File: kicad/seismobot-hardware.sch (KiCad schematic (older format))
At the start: 1 part

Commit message: raspberry pi header and mcu on schematic
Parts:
- added J?: Raspberry_Pi_2_3, symbol Connector:Raspberry_Pi_2_3
- added U?: STM32F051T8Yx, Package_CSP:ST_WLCSP-36_Die440, symbol MCU_ST_STM32F0:STM32F051T8Yx
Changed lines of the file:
@@
+	1    0    0    -1
+$EndComp
+$Comp
+L Connector:Raspberry_Pi_2_3 J?
+U 1 1 6092C0A8
+P 6300 3700
+F 0 "J?" H 6300 5181 50  0000 C CNN
+F 1 "Raspberry_Pi_2_3" H 6300 5090 50  0000 C CNN
+F 2 "" H 6300 3700 50  0001 C CNN
+F 3 "https://www.raspberrypi.org/documentation/hardware/raspberrypi/schematics/rpi_SCH_3bplus_1p0_reduced.pdf" H 6300 3700 50  0001 C CNN
+	1    6300 3700
+	1    0    0    -1
+$EndComp
+$Comp
+L MCU_ST_STM32F0:STM32F051T8Yx U?
+U 1 1 609309D2
+P 2250 2100
+F 0 "U?" H 2200 911 50  0000 C CNN
+F 1 "STM32F051T8Yx" H 2200 820 50  0000 C CNN
+F 2 "Package_CSP:ST_WLCSP-36_Die440" H 1750 1100 50  0001 R CNN
+F 3 "http://www.st.com/st-web-ui/static/active/en/resource/technical/document/datasheet/DM00039193.pdf" H 2250 2100 50  0001 C CNN
+	1    2250 2100
 	1    0    0    -1
 $EndComp

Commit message: add MCU (ATSAMD09) and supporting circuitry
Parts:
- removed U?: STM32F051T8Yx, Package_CSP:ST_WLCSP-36_Die440, symbol MCU_ST_STM32F0:STM32F051T8Yx
- added C?: 4.7 uF, symbol Device:C
- added C?: 0.1 uF, symbol Device:C
- added D?: LED, symbol Device:LED
- added R?: 1k, symbol Device:R
- added R?: 100, symbol Device:R
- added U?: ATSAMD09C13A-SS, Package_SO:SOIC-14_3.9x8.7mm_P1.27mm, symbol MCU_Microchip_SAMD:ATSAMD09C13A-SS
- added Y?: 32768 Hz, symbol Device:Crystal
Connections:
- net labels added: +3V3, CS, GND, MISO, MOSI, RX, RxD, SCK, SWCLK, SWDIO, TX, TxD, ~RST
- wire segments 0 -> 52
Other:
- moved on the sheet: J?, U?

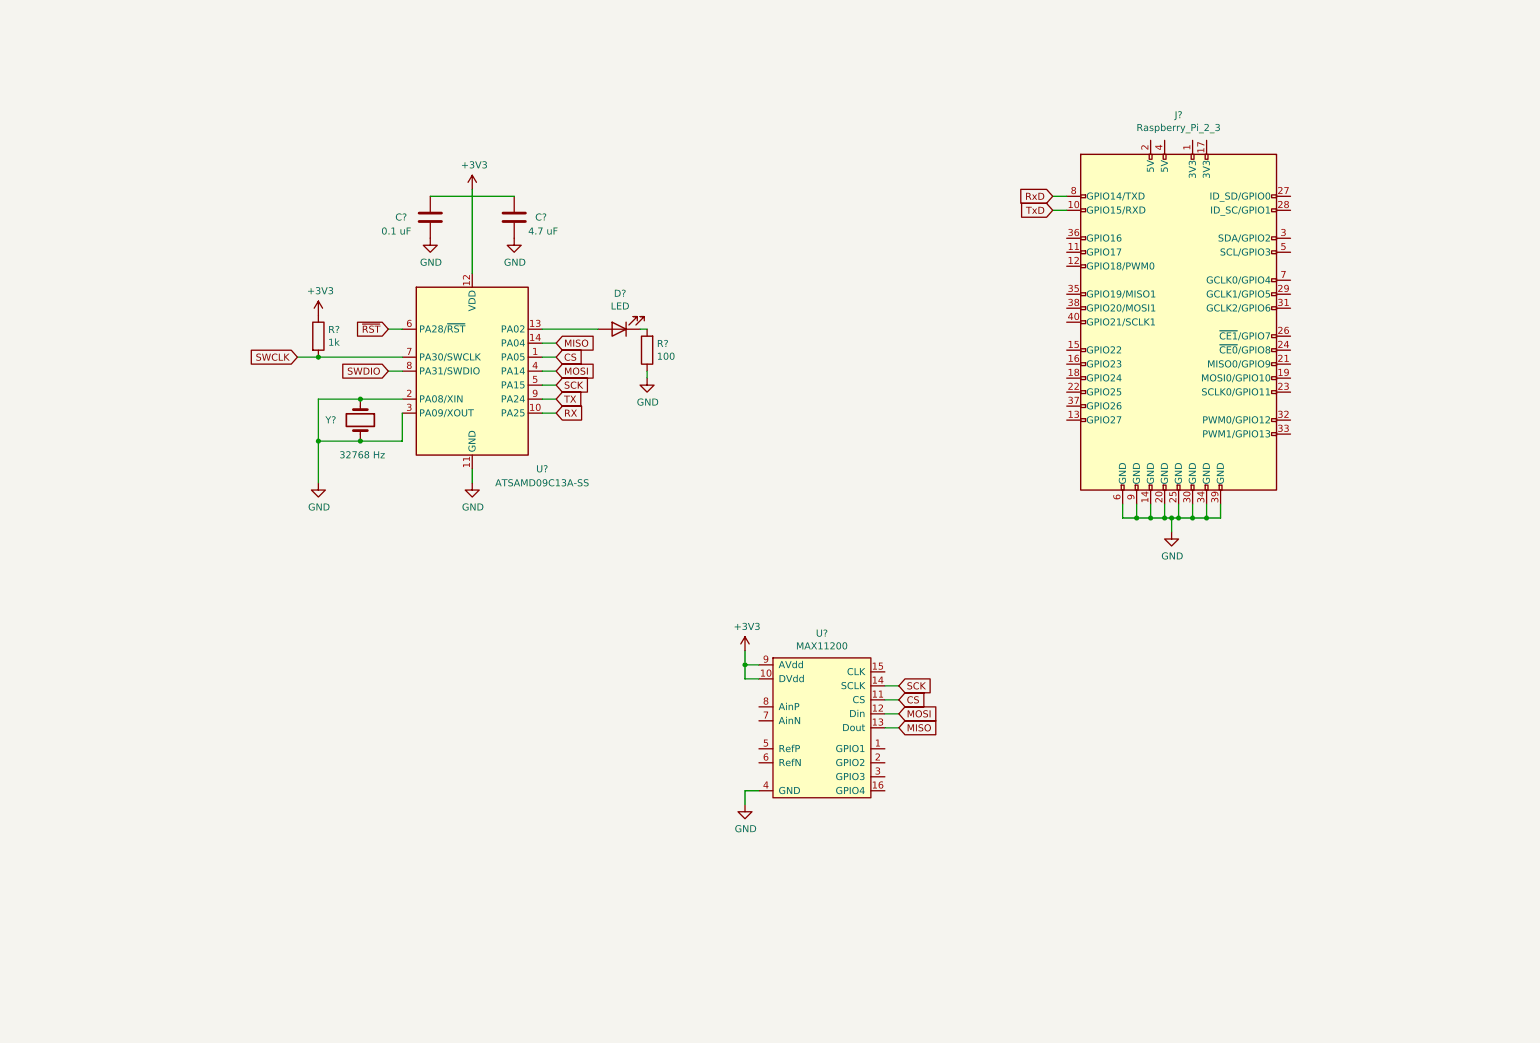
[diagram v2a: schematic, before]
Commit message: Added passives and clock to ADC
Based off of dev board
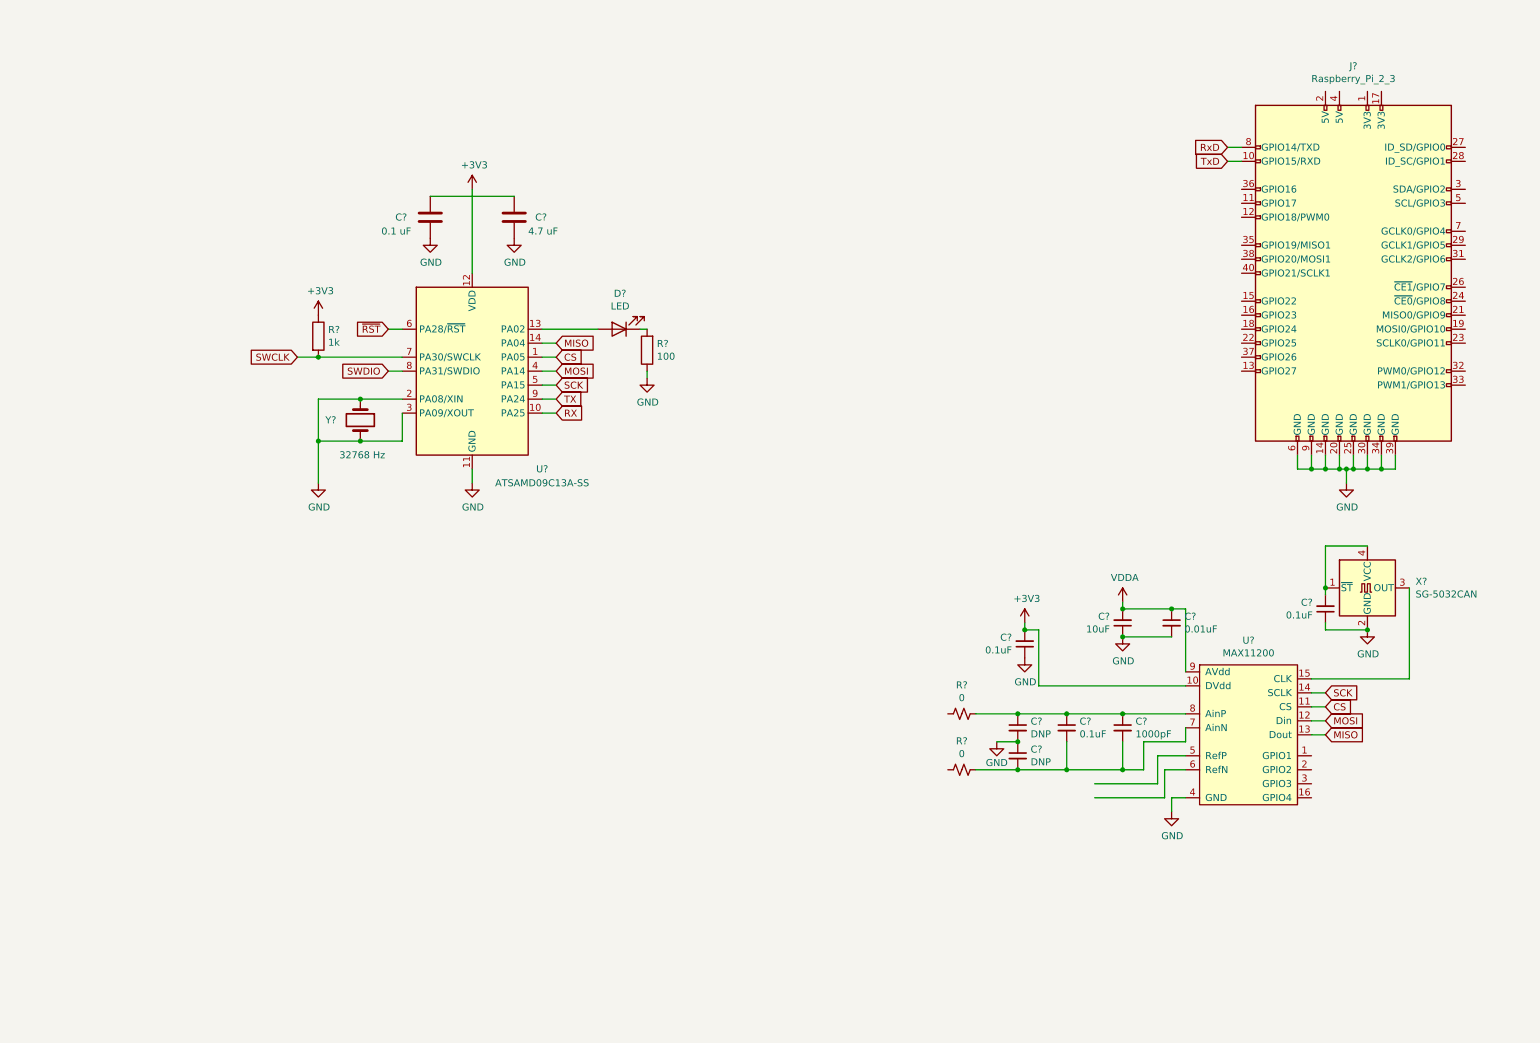
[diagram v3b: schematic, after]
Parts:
- added C?: 1000pF, symbol Device:C_Small
- added C? (x3): 0.1uF, symbol Device:C_Small
- added C?: 10uF, symbol Device:C_Small
- added C?: 0.01uF, symbol Device:C_Small
- added C? (x2): DNP, symbol Device:C_Small
- added R? (x2): 0, symbol Device:R_Small_US
- added X?: SG-5032CAN, Oscillator:Oscillator_SMD_SeikoEpson_SG8002LB-4Pin_5.0x3.2mm, symbol Oscillator:SG-5032CAN
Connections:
- net +3V3: now also C?.2; no longer U?.9 (AVdd)
- net GND: now also C?.1, C?.1, C?.1, C?.1, C?.2, C?.2, X?.2 (GND)
- net at U?.15 (CLK): now also X?.3 (OUT)
- net at U?.7 (AinN): now also C?.2, C?.2, C?.2, R?.1
- net at U?.8 (AinP): now also C?.1, C?.1, C?.1, R?.1
- new net: C?.2, X?.1 (~ST), X?.4 (VCC)
- new net VDDA: C?.1, C?.2, U?.9 (AVdd)
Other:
- moved on the sheet: J?, U?

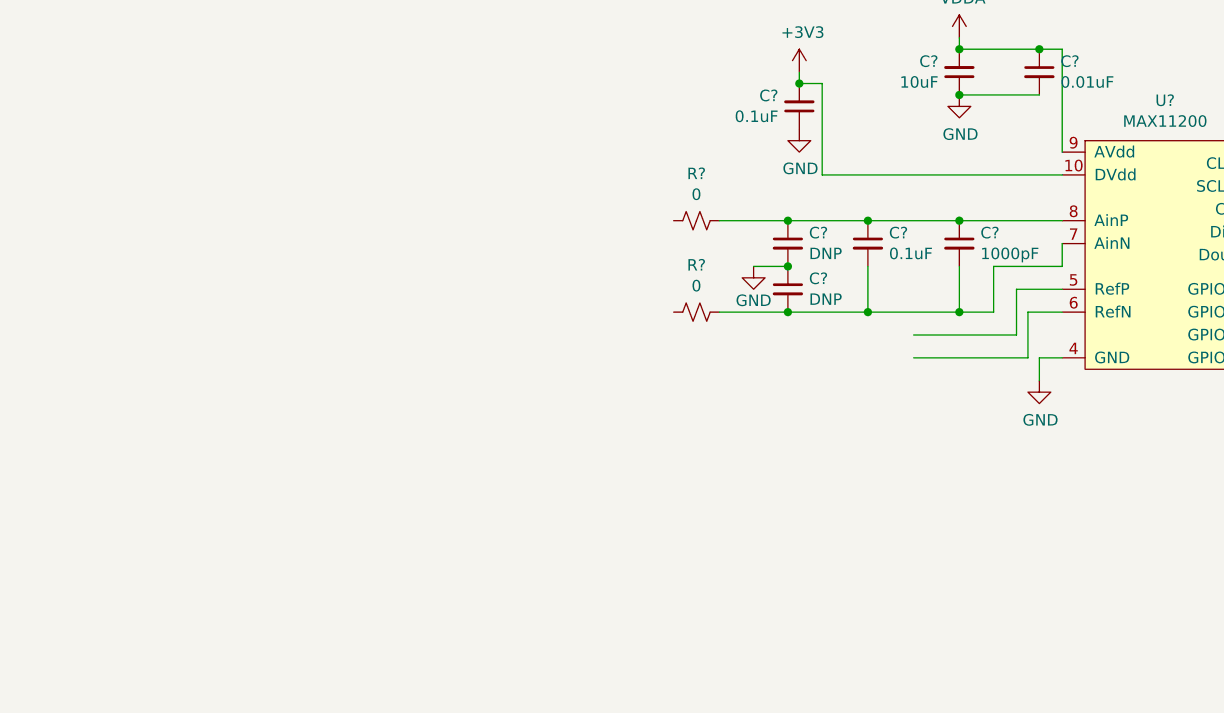
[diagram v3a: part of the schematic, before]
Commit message: added voltage references to schematic
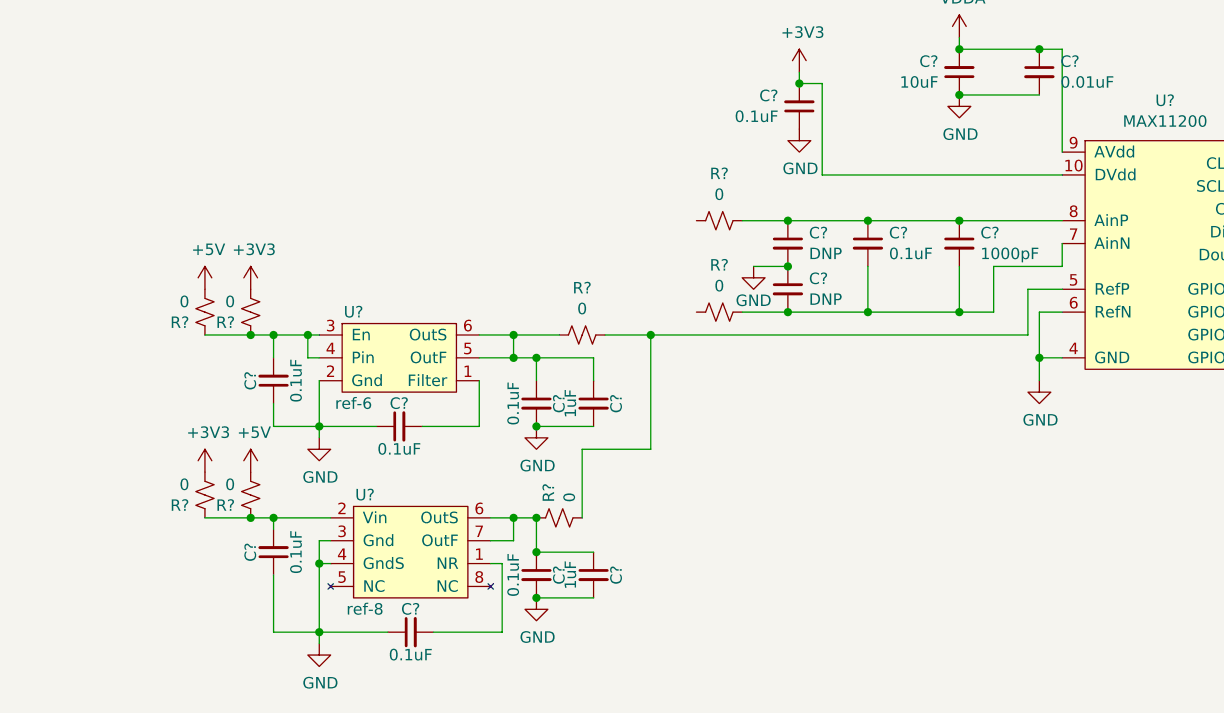
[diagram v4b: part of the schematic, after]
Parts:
- added C? (x6): 0.1uF, symbol Device:C_Small
- added C? (x2): 1uF, symbol Device:C_Small
- added R? (x6): 0, symbol Device:R_Small_US
- added U?: ref-6, symbol seismobot-hardware:ref-6
- added U?: ref-8, symbol seismobot-hardware:ref-8
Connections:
- net +3V3: now also R?.1, R?.1
- net GND: now also U?.6 (RefN), C?.1, C?.1, C?.1, C?.1, C?.2, C?.2, C?.2, C?.2, U?.2 (Gnd), U?.3 (Gnd), U?.4 (GndS)
- net at U?.5 (RefP): now also R?.1, R?.1
- new net: C?.2, U?.1 (Filter)
- new net: C?.2, R?.2, R?.2, U?.3 (En), U?.4 (Pin)
- new net: C?.1, C?.1, R?.2, U?.5 (OutF), U?.6 (OutS)
- new net: C?.2, U?.1 (NR)
- new net: C?.2, R?.2, R?.2, U?.2 (Vin)
- new net: C?.1, C?.1, R?.2, U?.6 (OutS), U?.7 (OutF)
- new net +5V: R?.1, R?.1
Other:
- moved on the sheet: R?

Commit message: add input stage 1
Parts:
- added C? (x2): 1n, symbol Device:C_Small
- added C? (x3): 10u, symbol Device:C_Small
- added C?: 10n, symbol Device:C_Small
- added C?: 0.1u, symbol Device:C_Small
- added J?: Screw_Terminal_01x02, symbol Connector:Screw_Terminal_01x02
- added R?: 3.5, symbol Device:R_Small_US
- added R?: 200, symbol Device:R_Small_US
- added R? (x2): 32.88k, symbol Device:R_Small_US
- added R? (x2): 21, symbol Device:R_Small_US
- added R?: 99k, symbol Device:R_Small_US
- added R?: 150k, symbol Device:R_Small_US
- added R?: 5, symbol Device:R_Small_US
- added R?: 4k, symbol Device:R_Small_US
- added R? (x2): 5k, symbol Device:R_Small_US
- added R? (x2): 100, symbol Device:R_Small_US
- added R? (x2): 1k, symbol Device:R_Small_US
- added U? (x6): OPA2156xD, Package_SO:SOIC-8_3.9x4.9mm_P1.27mm, symbol Amplifier_Operational:OPA2156xD
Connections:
- net +3V3: now also U?.8 (V+), U?.8 (V+)
- net GND: now also C?.1, R?.1, R?.1, U?.4 (V-), U?.4 (V-)
- net RefP: now reaches R?.1, R?.1, U?.5 (RefP)
- net RefP: now also R?.2
- net at R?.2: now also R?.1 (x2)
- new net: C?.1, C?.2, R?.1, R?.2, R?.2, U?.1
- new net: C?.1, C?.2, J?.1 (Pin_1), R?.1, U?.2 (-)
- new net: C?.2, R?.1, R?.2, R?.2, U?.3 (+)
- new net: C?.2, R?.1, R?.2, U?.5 (+)
- new net: C?.1, J?.2 (Pin_2), R?.1, R?.2
- new net: C?.1, R?.1 (x2)
- new net: C?.2, R?.1, R?.2, R?.2, U?.1
- new net: C?.1, R?.1, R?.2, U?.2 (-)
- new net: C?.2, R?.2
- new net: R?.1, R?.2, U?.5 (+)
- new net: R?.1, R?.2, U?.6 (-)
- new net: R?.1, R?.2, U?.7
- new net 1.5v: C?.2, R?.2, R?.2, U?.3 (+), U?.6 (-), U?.7
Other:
- note added: "Negative Input"
- note added: "Positive Input"
